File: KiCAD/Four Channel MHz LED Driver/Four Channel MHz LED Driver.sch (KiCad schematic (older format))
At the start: 82 parts, among them J1 Barrel_Jack_Switch, J10 Conn_01x08_Female, J2 Conn_01x02_Female, J3 8P8C_Shielded_x4, J4 Conn_01x05_Female, J5 Conn_01x24_Female, J6 Conn_01x03_Male, J7 Conn_01x24_Female, J8 Conn_01x03_Female, J9 Conn_01x03_Female, M1 Fan_4pin, Q2 SUM70060E, SW1 SW_SPDT, SW2 Pushbutton_with_LED_-_ELUMOAT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, SW3 Pushbutton_with_LED_-_ELUMOAT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, SW4 Pushbutton_with_LED_-_ELUMOAT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, SW5 Pushbutton_with_LED_-_ELUMOAT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, U1 12V boost, U10 LT6200CS8-10, U14 Teensy3.6, U16 SN74LV4T125PWR, U2 ASSR-1218, U3 DPBW06F-05, U4 BDJ0GA5WEFJ-E2, U5 ADP7182AUJZ-1.8-R7, U6 TMUX1204DGSR, U7 ASSR-1218, U8 ASSR-1218, U9 ASSR-1218

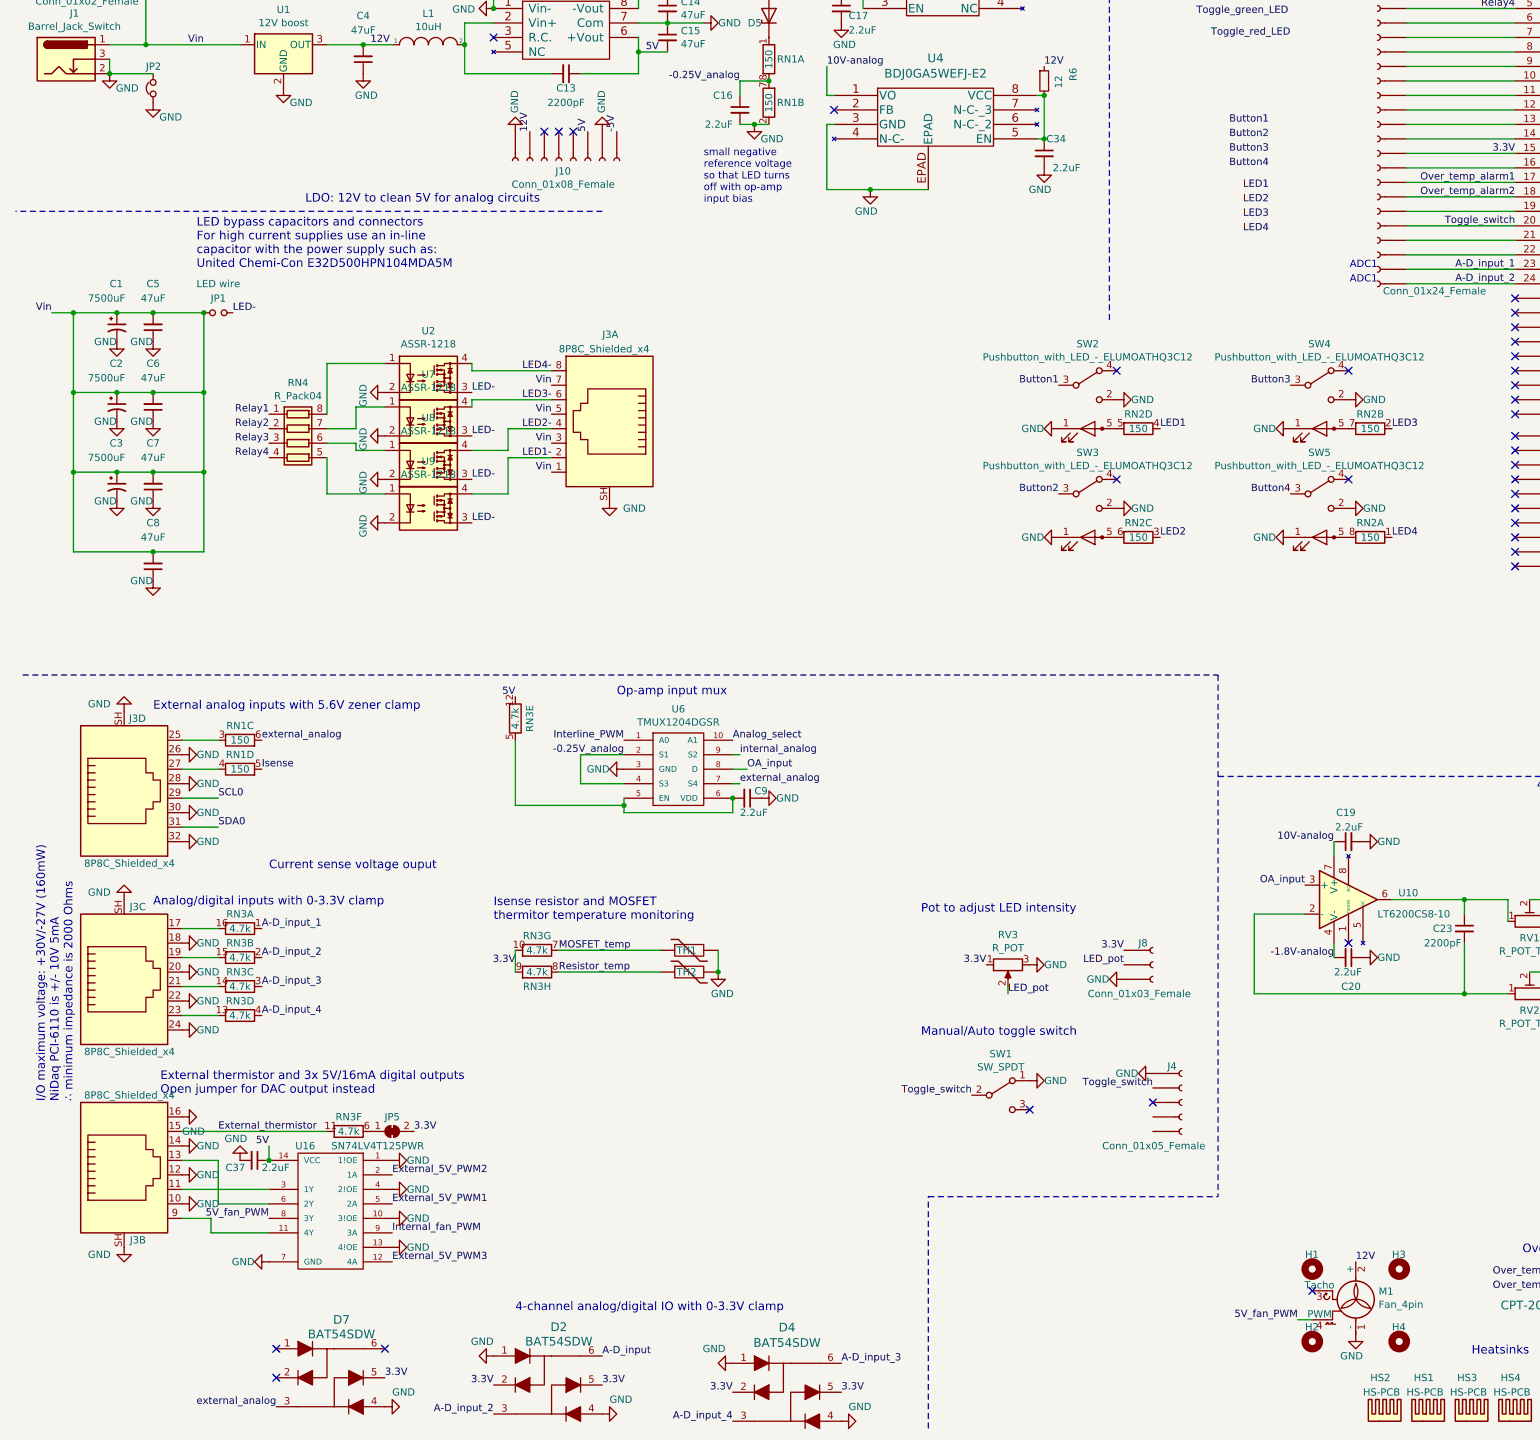
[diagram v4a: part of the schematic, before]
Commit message: Fan updated with bolts
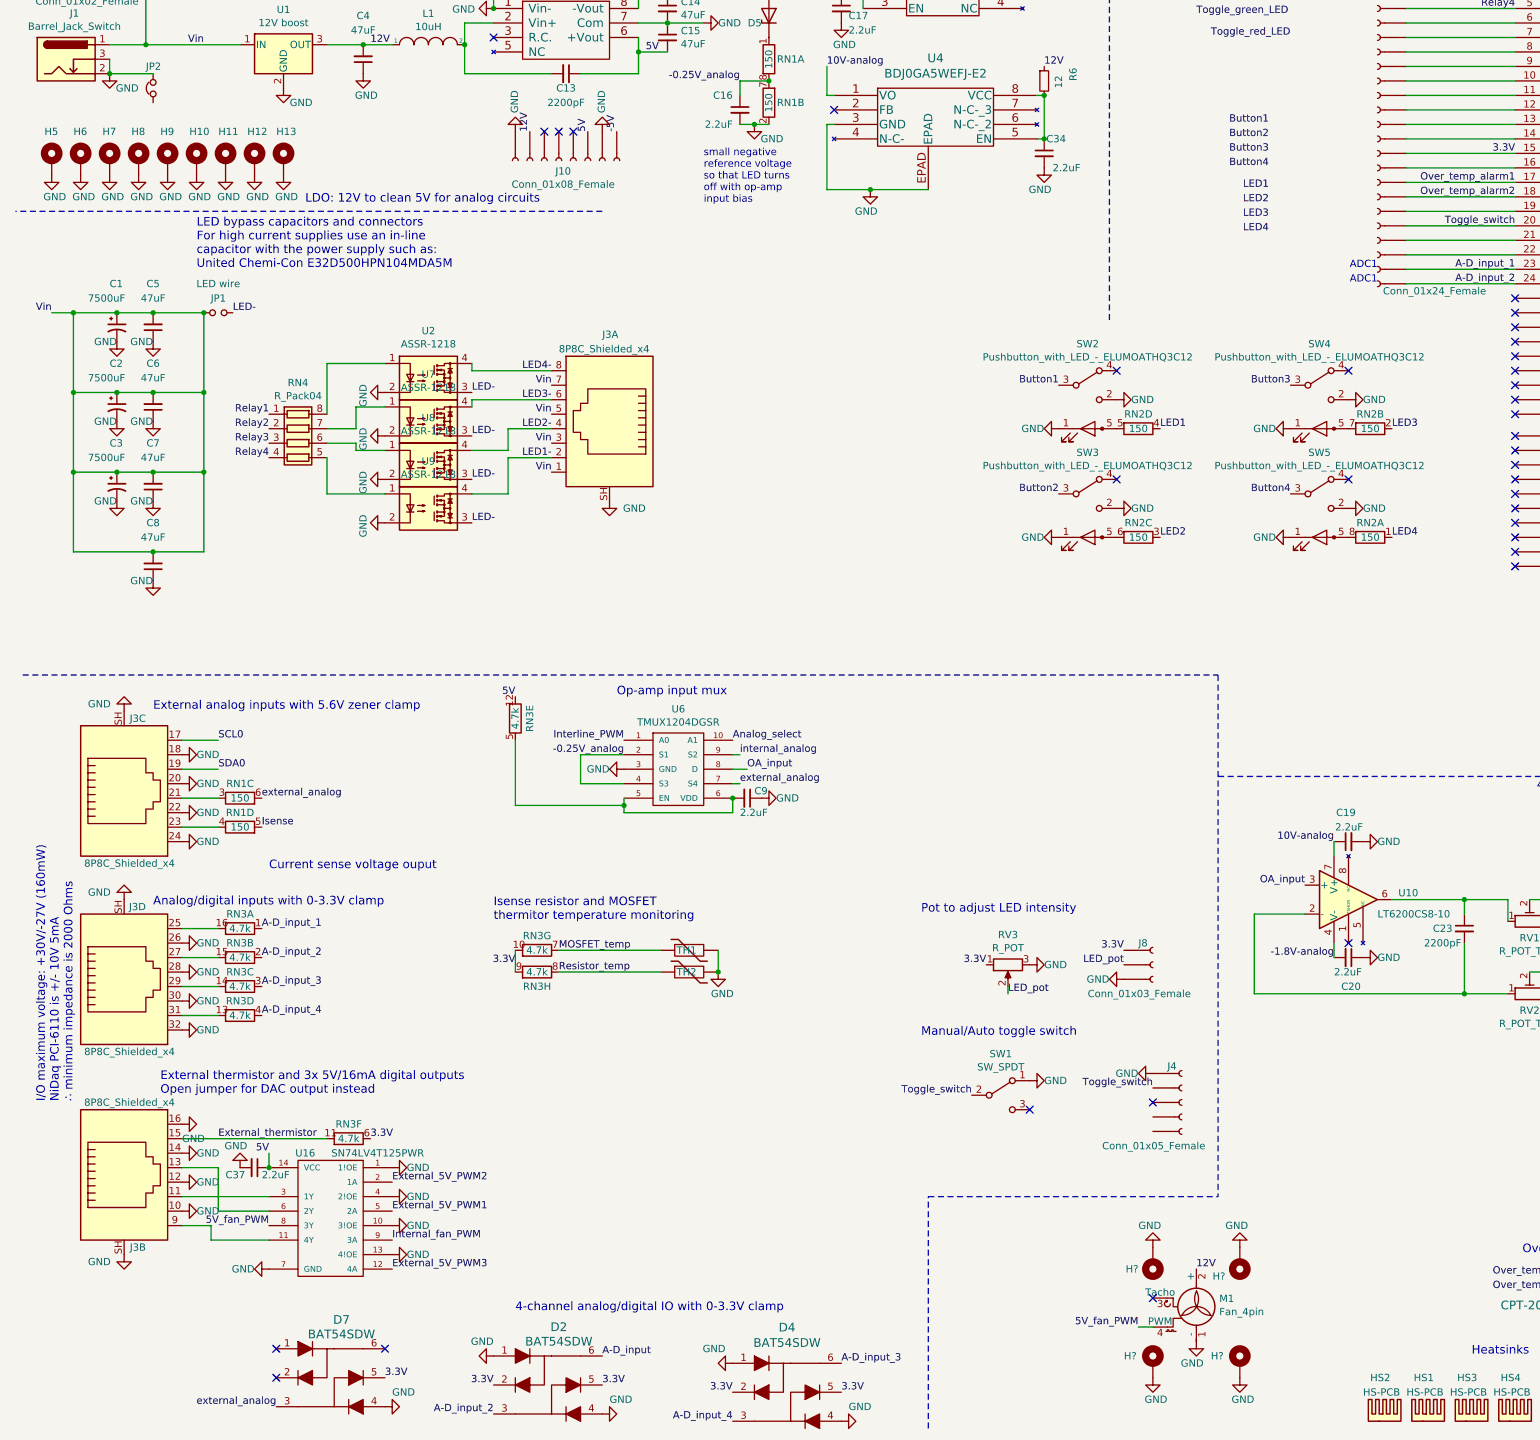
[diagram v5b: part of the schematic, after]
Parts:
- removed H1: MountingHole, Custom Footprints:90mm_fan_AFC0912DB-F00, symbol Mechanical:MountingHole
- removed H2, H3, H4: MountingHole, Custom Footprints:Ref_only, symbol Mechanical:MountingHole
- removed JP5: SolderJumper_2_Bridged, Jumper:SolderJumper-2_P1.3mm_Bridged_RoundedPad1.0x1.5mm, symbol Jumper:SolderJumper_2_Bridged
- added H10, H11, H12, H13, H5, H6, H7, H8, H9: MountingHole_Pad, Custom Footprints:Ground_Via, symbol Mechanical:MountingHole_Pad
- added H?: MountingHole_Pad, Custom Footprints:NF-A9_with_standoffs_and_bolts, symbol Mechanical:MountingHole_Pad
- added H? (x3): MountingHole_Pad, Custom Footprints:Ref_only, symbol Mechanical:MountingHole_Pad
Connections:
- net 3.3V: now also RN3.6 (R6.1)
- net GND: now also J3.18, J3.20, J3.22, J3.24, J3.26, J3.28, J3.30, J3.32, H10.1, H11.1, H12.1, H13.1, H5.1, H6.1, H7.1, H8.1, H9.1, H?.1, H?.1, H?.1, H?.1; no longer J3.18, J3.20, J3.22, J3.24, J3.26, J3.28, J3.30, J3.32, JP2.1
- net SCL0: now also J3.17; no longer J3.29
- net SDA0: now also J3.19; no longer J3.31
- net at RN1.3 (R3.1): now also J3.21; no longer J3.25
- net at RN1.4 (R4.1): now also J3.23; no longer J3.27
- net at RN3.16 (R1.2): now also J3.25; no longer J3.17
- net at RN3.15 (R2.2): now also J3.27; no longer J3.19
- net at RN3.14 (R3.2): now also J3.29; no longer J3.21
- net at RN3.13 (R4.2): now also J3.31; no longer J3.23
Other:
- moved on the sheet: C37, J3B, M1, RN1C, RN1D, RN3F, U16

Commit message: Improved jumper
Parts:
- JP2: Manufacturer Stackpole Electronics Inc -> Keystone Electronics; Part # RMCF1206ZT0R00 -> 5108
- gave numbers to parts that had none: 4
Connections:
- net GND: now also JP2.1
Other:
- note added: "See if there is a bigger zener set for D6 or split to 2 parts\n\nGND via - 9410-3ML and TIPS#15X1\n\nAdd shunt from Isense to fan post - https://www.digikey.com/product-detail/en/keystone-electronics/5104/36-5104-ND/4780769"
- note removed: "Use smaller LDOs - especially lower dropout on 10V rail\nUse lower wattage (smaller) resistor on 1.8V rail\nAdd RC filter to 12V input to 10V LDO\nRemove inductor and use same rail for 12V to 10V LDO?\nSee if there is a bigger zener set for D6 or split to 2 parts\n\nGND via - 9410-3ML and TIPS#15X1"
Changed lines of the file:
@@
 $EndComp
 Text Notes 4550 -50  0    118  ~ 0
-Use smaller LDOs - especially lower dropout on 10V rail\nUse lower wattage (smaller) resistor on 1.8V rail\nAdd RC filter to 12V input to 10V LDO\nRemove inductor and use same rail for 12V to 10V LDO?\nSee if there is a bigger zener set for D6 or split to 2 parts\n\nGND via - 9410-3ML and TIPS#15X1
+See if there is a bigger zener set for D6 or split to 2 parts\n\nGND via - 9410-3ML and TIPS#15X1\n\nAdd shunt from Isense to fan post - https://www.digikey.com/product-detail/en/keystone-electronics/5104/36-5104-ND/4780769
 Wire Wire Line
 	1350 1650 2000 1650
@@
 F 1 "Jumper_NC_Small" V 1355 1903 50  0001 R CNN
 F 2 "Resistor_SMD:R_1206_3216Metric" H 1400 1950 50  0001 C CNN
-F 3 "https://www.seielect.com/catalog/sei-rmcf_rmcp.pdf" H 1400 1950 50  0001 C CNN
-F 4 "Stackpole Electronics Inc" V 1400 1950 50  0001 C CNN "Manufacturer"
-F 5 "RMCF1206ZT0R00" V 1400 1950 50  0001 C CNN "Part #"
+F 3 "https://www.keyelco.com/userAssets/file/M65p54.pdf" H 1400 1950 50  0001 C CNN
+F 4 "Keystone Electronics" V 1400 1950 50  0001 C CNN "Manufacturer"
+F 5 "5108" V 1400 1950 50  0001 C CNN "Part #"
 	1    1400 1950
 	0    -1   -1   0
@@
 $EndComp
 $Comp
-L power:GND #PWR?
+L power:GND #PWR0173
 U 1 1 5FAFCBAE
 P 8900 9950
-F 0 "#PWR?" H 8900 9700 50  0001 C CNN
+F 0 "#PWR0173" H 8900 9700 50  0001 C CNN
 F 1 "GND" H 9000 9800 50  0000 R CNN
 F 2 "" H 8900 9950 50  0001 C CNN
@@
 $EndComp
 $Comp
-L Mechanical:MountingHole_Pad H?
+L Mechanical:MountingHole_Pad H3
 U 1 1 5FAFCBB6
 P 8900 10050
-F 0 "H?" H 9000 10150 50  0000 L CNN
+F 0 "H3" H 9000 10150 50  0000 L CNN
 F 1 "MountingHole_Pad" H 9000 10008 50  0001 L CNN
 F 2 "Custom Footprints:Ref_only" H 8900 10050 50  0001 C CNN
@@
 $EndComp
 $Comp
-L power:GND #PWR?
+L power:GND #PWR0174
 U 1 1 5FB0A3A7
 P 8300 10850
-F 0 "#PWR?" H 8300 10600 50  0001 C CNN
+F 0 "#PWR0174" H 8300 10600 50  0001 C CNN
 F 1 "GND" H 8400 10700 50  0000 R CNN
 F 2 "" H 8300 10850 50  0001 C CNN
@@
 $EndComp
 $Comp
-L Mechanical:MountingHole_Pad H?
+L Mechanical:MountingHole_Pad H2
 U 1 1 5FB0A3AF
 P 8300 10750
-F 0 "H?" H 8100 10800 50  0000 L CNN
+F 0 "H2" H 8100 10800 50  0000 L CNN
 F 1 "MountingHole_Pad" H 8400 10708 50  0001 L CNN
 F 2 "Custom Footprints:Ref_only" H 8300 10750 50  0001 C CNN
@@
 $EndComp
 $Comp
-L power:GND #PWR?
+L power:GND #PWR0175
 U 1 1 5FB1B0A7
 P 8900 10850
-F 0 "#PWR?" H 8900 10600 50  0001 C CNN
+F 0 "#PWR0175" H 8900 10600 50  0001 C CNN
 F 1 "GND" H 9000 10700 50  0000 R CNN
 F 2 "" H 8900 10850 50  0001 C CNN
@@
 $EndComp
 $Comp
-L Mechanical:MountingHole_Pad H?
+L Mechanical:MountingHole_Pad H4
 U 1 1 5FB1B0AF
 P 8900 10750
-F 0 "H?" H 8700 10800 50  0000 L CNN
+F 0 "H4" H 8700 10800 50  0000 L CNN
 F 1 "MountingHole_Pad" H 9000 10708 50  0001 L CNN
 F 2 "Custom Footprints:Ref_only" H 8900 10750 50  0001 C CNN
@@
 $EndComp
 $Comp
-L Mechanical:MountingHole_Pad H?
+L Mechanical:MountingHole_Pad H1
 U 1 1 5FACF30E
 P 8300 10050
-F 0 "H?" H 8400 10100 50  0000 L CNN
+F 0 "H1" H 8400 10100 50  0000 L CNN
 F 1 "MountingHole_Pad" H 8400 10008 50  0001 L CNN
 F 2 "Custom Footprints:NF-A9_with_standoffs_and_bolts" H 8300 10050 50  0001 C CNN
@@
 $EndComp
 $Comp
-L power:GND #PWR?
+L power:GND #PWR0177
 U 1 1 5FACF308
 P 8300 9950
-F 0 "#PWR?" H 8300 9700 50  0001 C CNN
+F 0 "#PWR0177" H 8300 9700 50  0001 C CNN
 F 1 "GND" H 8400 9800 50  0000 R CNN
 F 2 "" H 8300 9950 50  0001 C CNN
@@
 	1    0    0    -1
 $EndComp
+$Comp
+L power:GND #PWR?
+U 1 1 5FC416EF
+P 1400 2050
+F 0 "#PWR?" H 1400 1800 50  0001 C CNN
+F 1 "GND" H 1600 1950 50  0000 R CNN
+F 2 "" H 1400 2050 50  0001 C CNN
+F 3 "" H 1400 2050 50  0001 C CNN
+	1    1400 2050
+	1    0    0    -1
+$EndComp
